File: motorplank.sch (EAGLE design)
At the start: 13 parts, among them IC1 74AHC1G86DBV

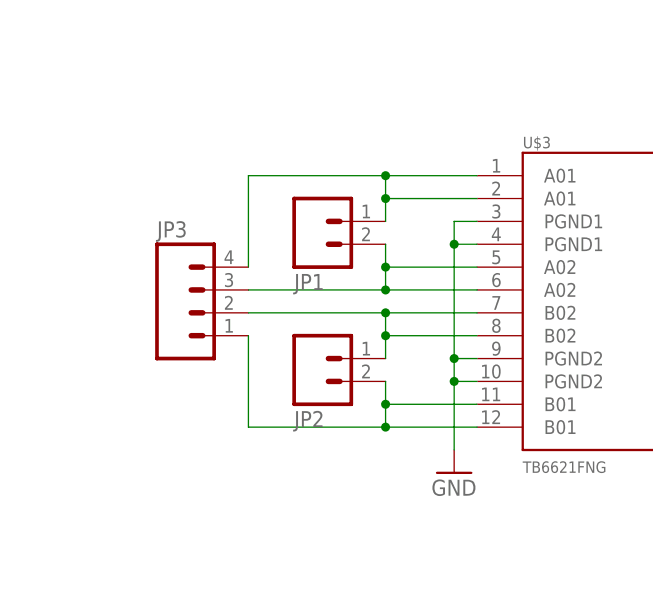
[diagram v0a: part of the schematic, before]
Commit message: Add LED indicators for motor outputs.
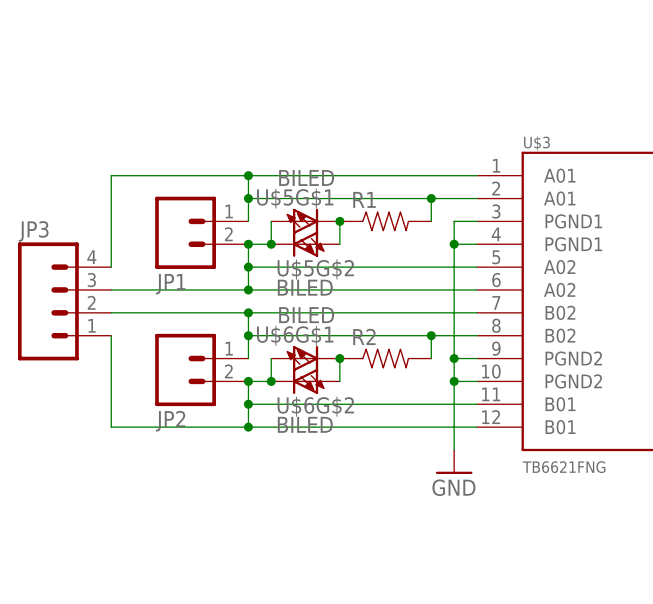
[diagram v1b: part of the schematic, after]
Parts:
- added R1, R2: (no value), SparkFun-Passives:RESISTOR0805-RES
- added U$5, U$6: BILED, nickparts:BILED
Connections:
- removed net N$28: JP2.2, JP3.1, U$3.B01@11, U$3.B01@12
- removed net N$30: JP1.2, JP3.3, U$3.A02@5, U$3.A02@6
- new net N$33: R1.1, U$5G$1.C, U$5G$2.A
- new net N$34: R2.1, U$6G$1.C, U$6G$2.A
- new net N$35: JP1.2, JP3.3, U$3.A02@5, U$3.A02@6, U$5G$1.A, U$5G$2.C
- new net N$36: JP2.2, JP3.1, U$3.B01@11, U$3.B01@12, U$6G$1.A, U$6G$2.C
- net N$27: now also R2.2
- net N$29: now also R1.2
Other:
- moved on the sheet: JP1, JP2, JP3
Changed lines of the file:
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@@
 <part name="GND9" library="supply1" deviceset="GND" device=""/>
 <part name="+3V5" library="supply1" deviceset="+3V3" device=""/>
+<part name="U$5" library="nickparts" deviceset="BILED" device=""/>
+<part name="U$6" library="nickparts" deviceset="BILED" device=""/>
+<part name="R1" library="SparkFun-Passives" deviceset="RESISTOR" device="0805-RES"/>
+<part name="R2" library="SparkFun-Passives" deviceset="RESISTOR" device="0805-RES"/>
 </parts>
 <sheets>
@@
 <instance part="GND4" gate="1" x="86.36" y="25.4"/>
 <instance part="U$3" gate="G$1" x="-71.12" y="38.1"/>
-<instance part="JP1" gate="G$1" x="-106.68" y="45.72" rot="MR180"/>
-<instance part="JP2" gate="G$1" x="-106.68" y="30.48" rot="MR180"/>
-<instance part="JP3" gate="G$1" x="-119.38" y="35.56"/>
+<instance part="JP1" gate="G$1" x="-121.92" y="45.72" rot="MR180"/>
+<instance part="JP2" gate="G$1" x="-121.92" y="30.48" rot="MR180"/>
+<instance part="JP3" gate="G$1" x="-134.62" y="35.56"/>
 <instance part="GND5" gate="1" x="-91.44" y="17.78"/>
 <instance part="JP4" gate="G$1" x="0" y="-17.78"/>
@@
 <instance part="GND9" gate="1" x="-101.6" y="78.74"/>
 <instance part="+3V5" gate="G$1" x="-88.9" y="99.06"/>
+<instance part="U$5" gate="G$1" x="-106.68" y="45.72" rot="R90"/>
+<instance part="U$5" gate="G$2" x="-109.22" y="43.18" rot="R270"/>
+<instance part="U$6" gate="G$1" x="-106.68" y="30.48" rot="R90"/>
+<instance part="U$6" gate="G$2" x="-109.22" y="27.94" rot="R270"/>
+<instance part="R1" gate="G$1" x="-99.06" y="45.72"/>
+<instance part="R2" gate="G$1" x="-99.06" y="30.48"/>
 </instances>
 <busses>
@@
 <pinref part="U$3" gate="G$1" pin="B02@8"/>
 <pinref part="JP2" gate="G$1" pin="1"/>
-<wire x1="-88.9" y1="33.02" x2="-99.06" y2="33.02" width="0.1524" layer="91"/>
-<wire x1="-99.06" y1="33.02" x2="-99.06" y2="30.48" width="0.1524" layer="91"/>
+<wire x1="-88.9" y1="33.02" x2="-93.98" y2="33.02" width="0.1524" layer="91"/>
+<wire x1="-93.98" y1="33.02" x2="-114.3" y2="33.02" width="0.1524" layer="91"/>
+<wire x1="-114.3" y1="33.02" x2="-114.3" y2="30.48" width="0.1524" layer="91"/>
 <pinref part="U$3" gate="G$1" pin="B02@7"/>
-<wire x1="-88.9" y1="35.56" x2="-99.06" y2="35.56" width="0.1524" layer="91"/>
-<wire x1="-99.06" y1="35.56" x2="-99.06" y2="33.02" width="0.1524" layer="91"/>
-<junction x="-99.06" y="33.02"/>
+<wire x1="-88.9" y1="35.56" x2="-114.3" y2="35.56" width="0.1524" layer="91"/>
+<wire x1="-114.3" y1="35.56" x2="-114.3" y2="33.02" width="0.1524" layer="91"/>
+<junction x="-114.3" y="33.02"/>
 <pinref part="JP3" gate="G$1" pin="2"/>
-<wire x1="-114.3" y1="35.56" x2="-99.06" y2="35.56" width="0.1524" layer="91"/>
-<junction x="-99.06" y="35.56"/>
-</segment>
-</net>
-<net name="N$28" class="0">
-<segment>
-<pinref part="U$3" gate="G$1" pin="B01@11"/>
-<pinref part="JP2" gate="G$1" pin="2"/>
-<wire x1="-88.9" y1="25.4" x2="-99.06" y2="25.4" width="0.1524" layer="91"/>
-<wire x1="-99.06" y1="25.4" x2="-99.06" y2="27.94" width="0.1524" layer="91"/>
-<pinref part="U$3" gate="G$1" pin="B01@12"/>
-<wire x1="-88.9" y1="22.86" x2="-99.06" y2="22.86" width="0.1524" layer="91"/>
-<wire x1="-99.06" y1="22.86" x2="-99.06" y2="25.4" width="0.1524" layer="91"/>
-<junction x="-99.06" y="25.4"/>
-<pinref part="JP3" gate="G$1" pin="1"/>
-<wire x1="-99.06" y1="22.86" x2="-114.3" y2="22.86" width="0.1524" layer="91"/>
-<wire x1="-114.3" y1="22.86" x2="-114.3" y2="33.02" width="0.1524" layer="91"/>
-<junction x="-99.06" y="22.86"/>
+<wire x1="-129.54" y1="35.56" x2="-114.3" y2="35.56" width="0.1524" layer="91"/>
+<junction x="-114.3" y="35.56"/>
+<pinref part="R2" gate="G$1" pin="2"/>
+<wire x1="-93.98" y1="30.48" x2="-93.98" y2="33.02" width="0.1524" layer="91"/>
+<junction x="-93.98" y="33.02"/>
 </segment>
 </net>
@@
 <pinref part="U$3" gate="G$1" pin="A01@1"/>
 <pinref part="JP1" gate="G$1" pin="1"/>
-<wire x1="-88.9" y1="50.8" x2="-99.06" y2="50.8" width="0.1524" layer="91"/>
-<wire x1="-99.06" y1="50.8" x2="-99.06" y2="48.26" width="0.1524" layer="91"/>
+<wire x1="-88.9" y1="50.8" x2="-114.3" y2="50.8" width="0.1524" layer="91"/>
+<wire x1="-114.3" y1="50.8" x2="-114.3" y2="48.26" width="0.1524" layer="91"/>
 <pinref part="U$3" gate="G$1" pin="A01@2"/>
-<wire x1="-99.06" y1="48.26" x2="-99.06" y2="45.72" width="0.1524" layer="91"/>
-<wire x1="-88.9" y1="48.26" x2="-99.06" y2="48.26" width="0.1524" layer="91"/>
-<junction x="-99.06" y="48.26"/>
+<wire x1="-114.3" y1="48.26" x2="-114.3" y2="45.72" width="0.1524" layer="91"/>
+<wire x1="-88.9" y1="48.26" x2="-93.98" y2="48.26" width="0.1524" layer="91"/>
+<junction x="-114.3" y="48.26"/>
 <pinref part="JP3" gate="G$1" pin="4"/>
-<wire x1="-99.06" y1="50.8" x2="-114.3" y2="50.8" width="0.1524" layer="91"/>
-<wire x1="-114.3" y1="50.8" x2="-114.3" y2="40.64" width="0.1524" layer="91"/>
-<junction x="-99.06" y="50.8"/>
-</segment>
-</net>
-<net name="N$30" class="0">
-<segment>
-<pinref part="U$3" gate="G$1" pin="A02@5"/>
-<pinref part="JP1" gate="G$1" pin="2"/>
-<wire x1="-88.9" y1="40.64" x2="-99.06" y2="40.64" width="0.1524" layer="91"/>
-<wire x1="-99.06" y1="40.64" x2="-99.06" y2="43.18" width="0.1524" layer="91"/>
-<pinref part="U$3" gate="G$1" pin="A02@6"/>
-<wire x1="-88.9" y1="38.1" x2="-99.06" y2="38.1" width="0.1524" layer="91"/>
-<wire x1="-99.06" y1="38.1" x2="-99.06" y2="40.64" width="0.1524" layer="91"/>
-<junction x="-99.06" y="40.64"/>
-<pinref part="JP3" gate="G$1" pin="3"/>
-<wire x1="-114.3" y1="38.1" x2="-99.06" y2="38.1" width="0.1524" layer="91"/>
-<junction x="-99.06" y="38.1"/>
+<wire x1="-93.98" y1="48.26" x2="-114.3" y2="48.26" width="0.1524" layer="91"/>
+<wire x1="-114.3" y1="50.8" x2="-129.54" y2="50.8" width="0.1524" layer="91"/>
+<wire x1="-129.54" y1="50.8" x2="-129.54" y2="40.64" width="0.1524" layer="91"/>
+<junction x="-114.3" y="50.8"/>
+<pinref part="R1" gate="G$1" pin="2"/>
+<wire x1="-93.98" y1="45.72" x2="-93.98" y2="48.26" width="0.1524" layer="91"/>
+<junction x="-93.98" y="48.26"/>
 </segment>
 </net>
@@
 </segment>
 </net>
+<net name="N$33" class="0">
+<segment>
+<pinref part="U$5" gate="G$1" pin="C"/>
+<pinref part="R1" gate="G$1" pin="1"/>
+<pinref part="U$5" gate="G$2" pin="A"/>
+<wire x1="-104.14" y1="43.18" x2="-104.14" y2="45.72" width="0.1524" layer="91"/>
+<junction x="-104.14" y="45.72"/>
+</segment>
+</net>
+<net name="N$34" class="0">
+<segment>
+<pinref part="U$6" gate="G$1" pin="C"/>
+<pinref part="R2" gate="G$1" pin="1"/>
+<pinref part="U$6" gate="G$2" pin="A"/>
+<wire x1="-104.14" y1="27.94" x2="-104.14" y2="30.48" width="0.1524" layer="91"/>
+<junction x="-104.14" y="30.48"/>
+</segment>
+</net>
+<net name="N$35" class="0">
+<segment>
+<pinref part="U$5" gate="G$1" pin="A"/>
+<pinref part="U$5" gate="G$2" pin="C"/>
+<wire x1="-111.76" y1="45.72" x2="-111.76" y2="43.18" width="0.1524" layer="91"/>
+<pinref part="U$3" gate="G$1" pin="A02@5"/>
+<pinref part="JP1" gate="G$1" pin="2"/>
+<wire x1="-88.9" y1="40.64" x2="-114.3" y2="40.64" width="0.1524" layer="91"/>
+<wire x1="-114.3" y1="40.64" x2="-114.3" y2="43.18" width="0.1524" layer="91"/>
+<pinref part="U$3" gate="G$1" pin="A02@6"/>
+<wire x1="-88.9" y1="38.1" x2="-114.3" y2="38.1" width="0.1524" layer="91"/>
+<wire x1="-114.3" y1="38.1" x2="-114.3" y2="40.64" width="0.1524" layer="91"/>
+<junction x="-114.3" y="40.64"/>
+<pinref part="JP3" gate="G$1" pin="3"/>
+<wire x1="-129.54" y1="38.1" x2="-114.3" y2="38.1" width="0.1524" layer="91"/>
+<junction x="-114.3" y="38.1"/>
+<wire x1="-111.76" y1="43.18" x2="-114.3" y2="43.18" width="0.1524" layer="91"/>
+<junction x="-111.76" y="43.18"/>
+<junction x="-114.3" y="43.18"/>
+</segment>
+</net>
+<net name="N$36" class="0">
+<segment>
+<pinref part="U$6" gate="G$1" pin="A"/>
+<pinref part="U$6" gate="G$2" pin="C"/>
+<wire x1="-111.76" y1="30.48" x2="-111.76" y2="27.94" width="0.1524" layer="91"/>
+<pinref part="U$3" gate="G$1" pin="B01@11"/>
+<pinref part="JP2" gate="G$1" pin="2"/>
+<wire x1="-88.9" y1="25.4" x2="-114.3" y2="25.4" width="0.1524" layer="91"/>
+<wire x1="-114.3" y1="25.4" x2="-114.3" y2="27.94" width="0.1524" layer="91"/>
+<pinref part="U$3" gate="G$1" pin="B01@12"/>
+<wire x1="-88.9" y1="22.86" x2="-114.3" y2="22.86" width="0.1524" layer="91"/>
+<wire x1="-114.3" y1="22.86" x2="-114.3" y2="25.4" width="0.1524" layer="91"/>
+<junction x="-114.3" y="25.4"/>
+<pinref part="JP3" gate="G$1" pin="1"/>
+<wire x1="-114.3" y1="22.86" x2="-129.54" y2="22.86" width="0.1524" layer="91"/>
+<wire x1="-129.54" y1="22.86" x2="-129.54" y2="33.02" width="0.1524" layer="91"/>
+<junction x="-114.3" y="22.86"/>
+<wire x1="-111.76" y1="27.94" x2="-114.3" y2="27.94" width="0.1524" layer="91"/>
+<junction x="-111.76" y="27.94"/>
+<junction x="-114.3" y="27.94"/>
+</segment>
+</net>
